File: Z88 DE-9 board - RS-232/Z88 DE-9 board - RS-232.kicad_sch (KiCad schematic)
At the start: 12 parts, among them J1 DE-9 PCB Mount, J2 D header

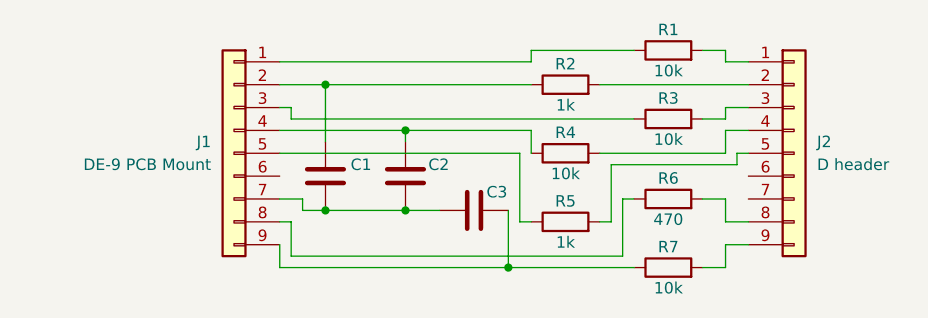
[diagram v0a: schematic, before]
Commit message: changed single-row header to dual so IDC connector can be used, replaced DE-9 footprint with custom to remove overhanging silkscreen
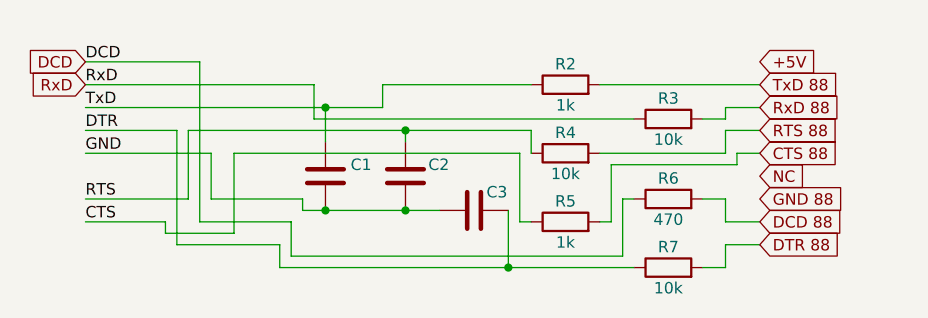
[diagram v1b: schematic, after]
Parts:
- removed J1: DE-9 PCB Mount, Connector_Dsub:DSUB-9_Female_Vertical_P2.77x2.84mm, symbol Connector_Generic:Conn_01x09
- removed J2: D header, Connector_PinHeader_2.54mm:PinHeader_1x09_P2.54mm_Vertical, symbol Connector_Generic:Conn_01x09
- removed R1: 10k, Resistor_SMD:R_0603_1608Metric_Pad0.98x0.95mm_HandSolder, symbol Device:R
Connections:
- net RTS: now reaches C2.1, R4.1
- net GND: now reaches C1.2, C2.2, C3.1
- net TxD: now reaches C1.1, R2.1
- net TxD 88: now reaches R2.2
- net RxD: now reaches R3.1
- net RxD 88: now reaches R3.2
- net CTS: now reaches R5.1
- net CTS 88: now reaches R5.2
- net DCD: now reaches R6.1
- net DTR: now reaches C3.2, R7.1
- net DTR 88: now reaches R7.2
- net RTS 88: now reaches R4.2
- net DCD 88: now reaches R6.2
